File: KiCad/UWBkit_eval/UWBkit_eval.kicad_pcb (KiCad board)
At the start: 2 copper layers, 49 x 60 mm, 46 parts, among them J2 Conn_BATT, J3 Conn_IO2, J4 Conn_IO1, J5 Conn_SWD, J6 Conn_RPI, J7 USB_C_Receptacle_USB2.0_14P, Q1 BSS341, Q2 BSS138, Q3 BSS138, SW1 SW_Push, SW2 SW_Push, U2 MAX40203AUK+T, U3 DWM3001C, U4 XC9285B33CMR-G, U6 IP4234CZ6

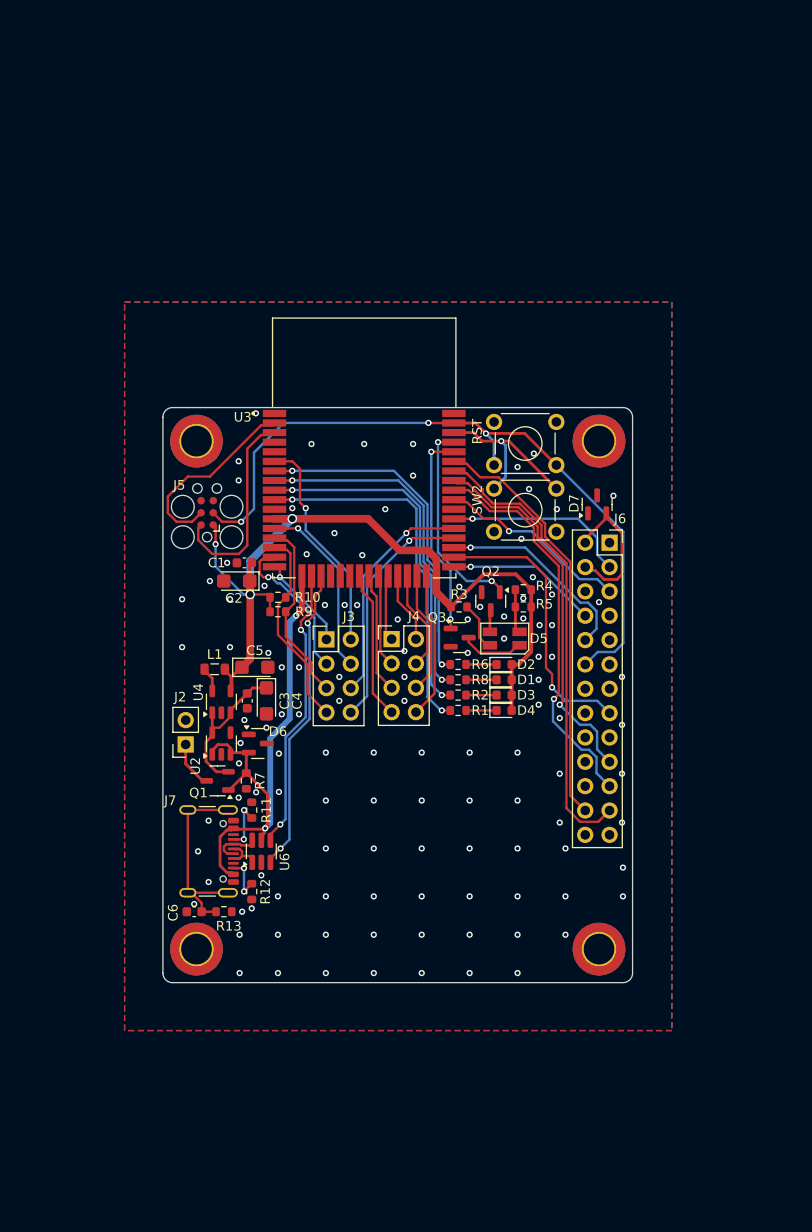
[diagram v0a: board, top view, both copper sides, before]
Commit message: Revised layout to be more compact
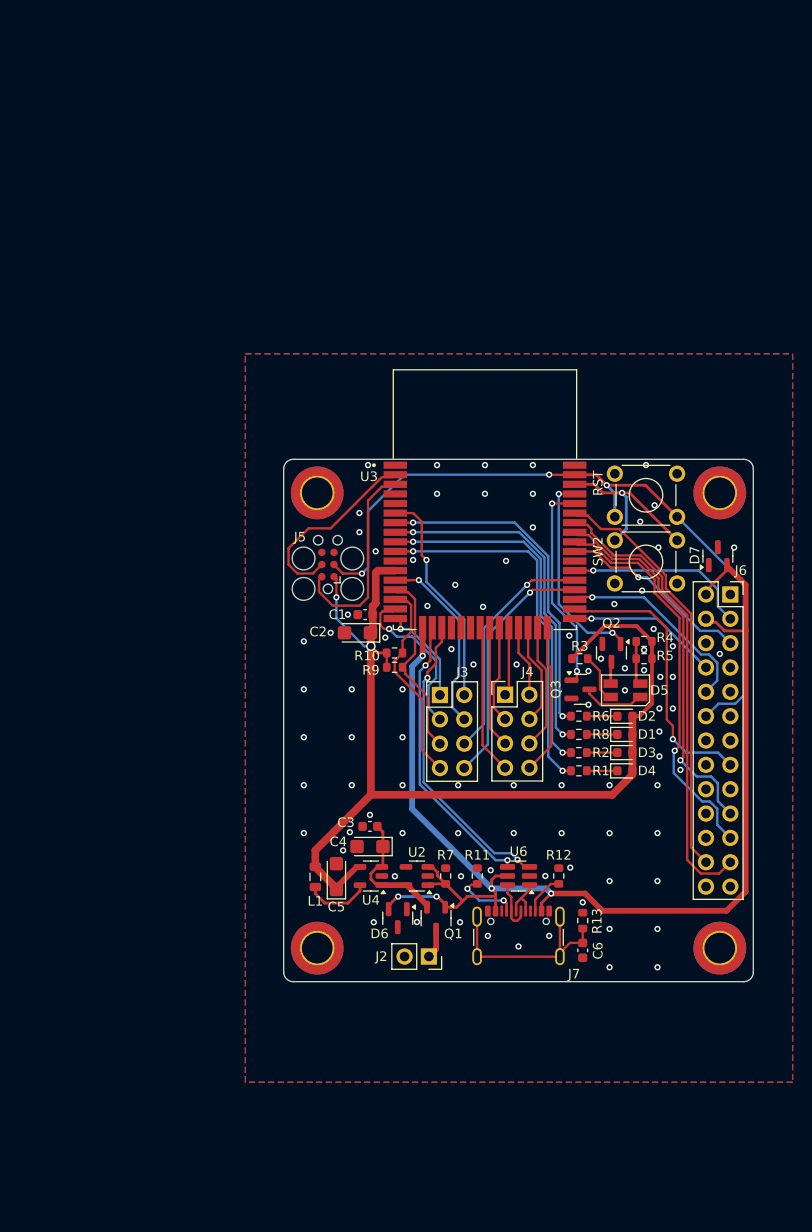
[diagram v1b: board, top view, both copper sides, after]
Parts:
- moved C6 40.7 mm to (157.8, 123.6), turned to -90 degrees
- moved R13 37.4 mm to (157.8, 120.5), turned to 90 degrees
- moved J7 34.9 mm to (151.1, 123.2), turned to 0 degrees
- moved J2 33.7 mm to (141.8, 124.3), turned to -90 degrees
- moved R12 32.1 mm to (155.3, 115.9), turned to 90 degrees
- moved U6 27.0 mm to (151.1, 115.9), turned to 180 degrees
- moved Q1 26.9 mm to (142.5, 120.3), turned to -90 degrees
- moved U2 24.6 mm to (140.5, 115.9), turned to 180 degrees
- moved R11 24.5 mm to (146.8, 115.9)
- moved L1 24.1 mm to (129.9, 116.0), turned to 90 degrees
- moved U4 24.0 mm to (135.7, 115.9), turned to 180 degrees
- moved C5 23.4 mm to (132.1, 115.9), turned to 90 degrees
- moved D6 23.4 mm to (138.5, 120.3), turned to -90 degrees
- moved R7 23.0 mm to (143.5, 115.9), turned to 90 degrees
- moved C4 18.6 mm to (135.6, 112.8), turned to 180 degrees
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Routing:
- net SOC_VBUS: track 71.8 -> 131.4 mm, vias 2 -> 5
- net +3V3: track 88.5 -> 109.8 mm, vias 3 -> 2
- net Net-(U4-Lx): track 2.60 -> 6.89 mm
- net Net-(Q1-S): track 16.3 -> 14.1 mm
- net V_BATT: track 4.95 -> 3.17 mm
- net Net-(J7-CC1): track 5.30 -> 6.72 mm
- net /IO_16: track 16.1 -> 17.2 mm
- net Net-(U3-P0.04): track 38.3 -> 39.1 mm
- net /IO_26: track 9.70 -> 10.5 mm
- net /DW_GP1: track 25.2 -> 25.9 mm
- net /DW_GP0: track 23.7 -> 24.5 mm
- net /TX_LED: track 21.6 -> 22.3 mm
- net /IO_13: track 18.9 -> 19.5 mm
- net /IO_17: track 10.0 -> 10.6 mm
- net /SOC_D+: track 32.2 -> 31.6 mm
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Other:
- board size 49 x 60 mm -> 49 x 54.5 mm

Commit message: Prepared PCB for RPI layout
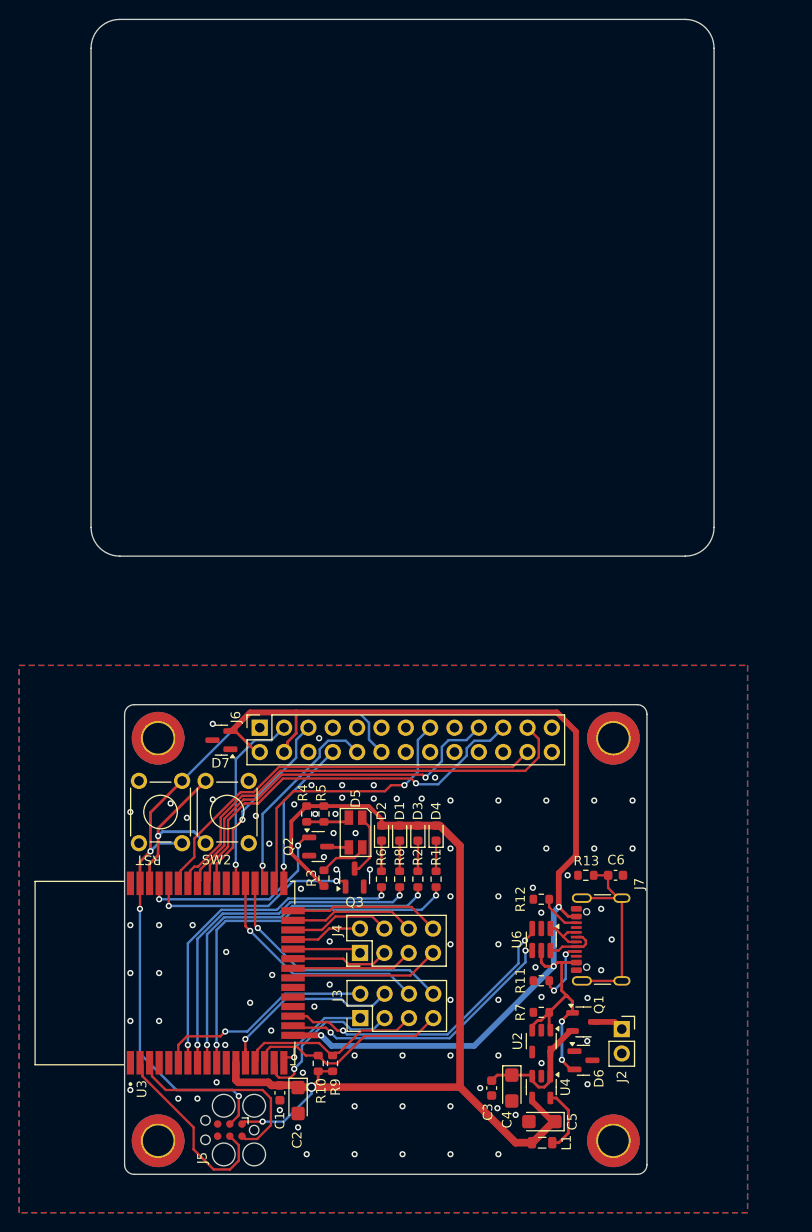
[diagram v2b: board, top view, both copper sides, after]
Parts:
- moved H1 69.6 mm to (113.5, 143.5), turned to 90 degrees
- moved H2 63.9 mm to (113.5, 101.5), turned to 90 degrees
- moved SW1 62.9 mm to (111.5, 112.5), turned to 90 degrees
- moved J5 59.9 mm to (121.0, 142.4), turned to 180 degrees
- moved U3 59.6 mm to (114.2, 126.0), turned to 90 degrees
- moved D7 55.2 mm to (120.1, 101.7), turned to 180 degrees
- moved J6 51.0 mm to (124.1, 100.4), turned to 90 degrees
- moved C1 50.7 mm to (126.2, 138.5), turned to -90 degrees
- moved SW2 49.2 mm to (123.0, 106.0), turned to -90 degrees
- moved C2 49.2 mm to (128.1, 139.3), turned to -90 degrees
- moved R10 43.6 mm to (130.2, 135.4), turned to -90 degrees
- moved R9 41.8 mm to (131.7, 135.4), turned to -90 degrees
- moved R4 39.5 mm to (129.0, 109.4), turned to -90 degrees
- moved R5 37.1 mm to (130.8, 109.4), turned to -90 degrees
- moved H3 36.9 mm to (161.0, 143.5), turned to 90 degrees
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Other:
- board size 49 x 54.5 mm -> 65 x 120.5 mm
